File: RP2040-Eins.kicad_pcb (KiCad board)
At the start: 2 copper layers, 68.6 x 53.3 mm, 57 parts, among them J1 Barrel_Jack_Switch, J10 USB_C_Receptacle_USB2.0, J2 CONN_I, J3 CONN_A, J4 CONN_P, J5 CONN_X, J7 CONN_JTAG, J8 CONN_D1, J9 CONN_D2, Q1 AO3401A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

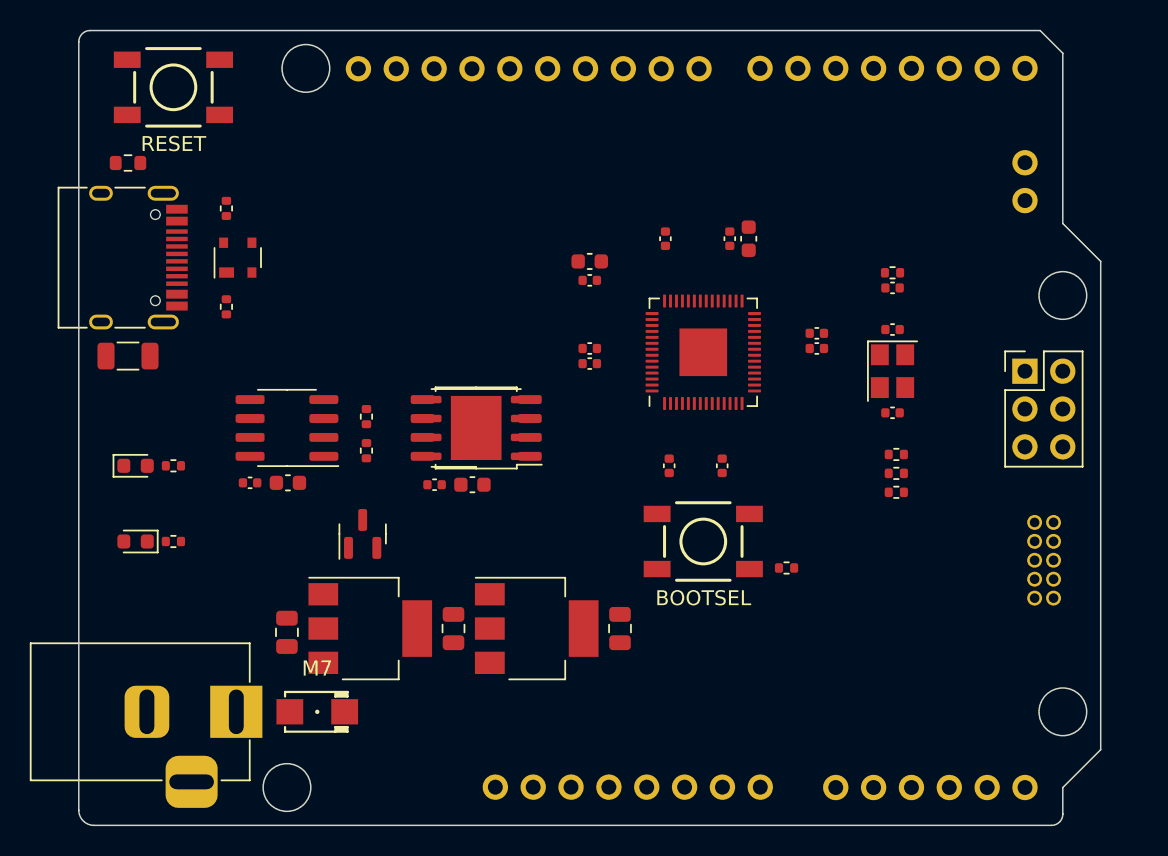
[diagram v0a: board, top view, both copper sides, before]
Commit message: Added few traces
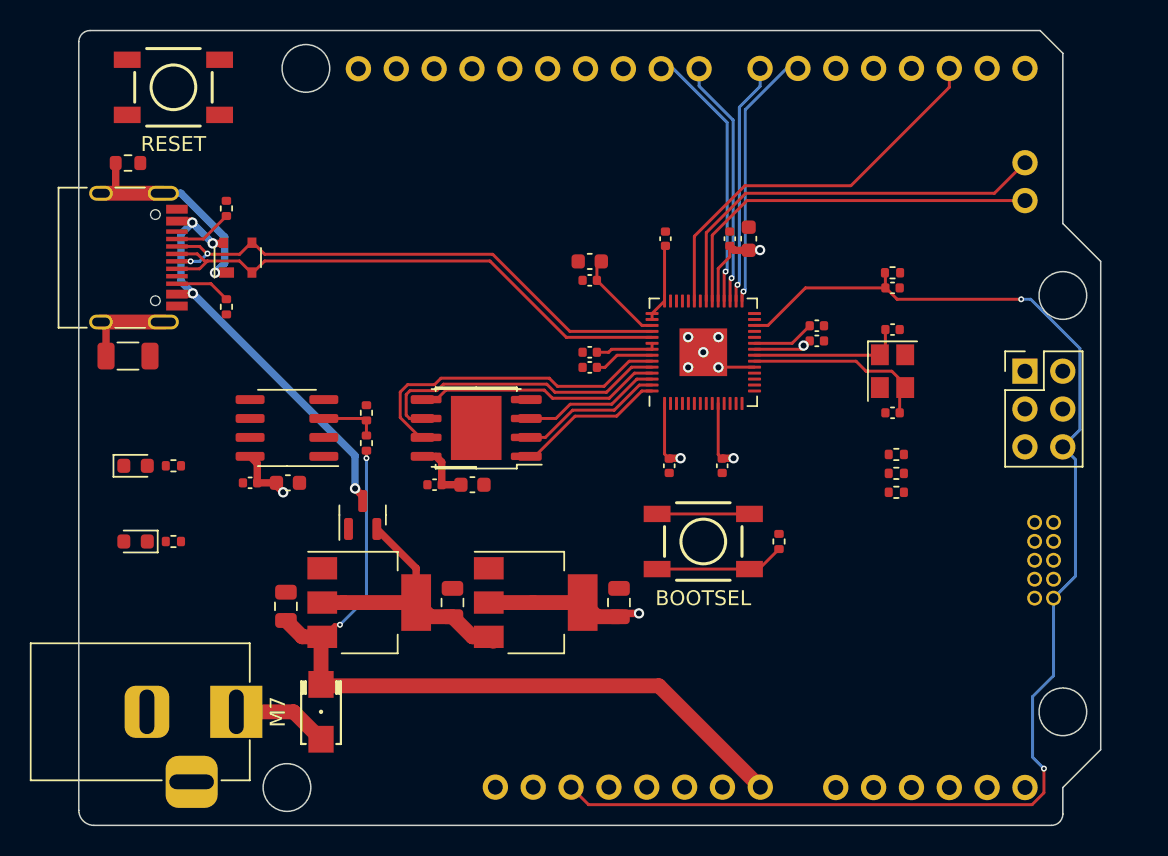
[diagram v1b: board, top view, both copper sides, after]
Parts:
- moved R7 1.85 mm to (174.0, 108.0), turned to 90 degrees
- moved C14 1.75 mm to (163.3, 112.0)
- moved U5 1.75 mm to (157.7, 112.0)
- moved C12 1.75 mm to (140.9, 112.3)
- moved C15 1.75 mm to (152.1, 112.0)
- moved U3 1.75 mm to (146.5, 112.0)
- moved Q1 1.27 mm to (146.1, 106.2)
- moved C7 0.51 mm to (176.5, 93.5)
- moved C6 0.51 mm to (176.5, 94.5)
- moved R8 0.51 mm to (146.3, 101.3)
- moved R9 0.26 mm to (146.3, 99.3)
- moved C10 0.25 mm to (161.3, 95.2)
- moved C22 0.25 mm to (161.3, 96.3)
- moved D4 0.25 mm to (143.3, 119.4), turned to -90 degrees
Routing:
- net RESET: track 0.00 -> 90.3 mm, vias 0 -> 2
- net VIN: track 0.00 -> 52.5 mm, vias 0 -> 2
- net +3V3: track 0.00 -> 42.7 mm, vias 0 -> 5
- net USB_DN: track 0.00 -> 37.2 mm, vias 0 -> 2
- net USB_DP: track 0.00 -> 37.1 mm
- net VBUS: track 0.00 -> 28.9 mm, vias 0 -> 4
- net D21: track 0.00 -> 27.9 mm
- net D2: track 0.00 -> 26.9 mm
- net D20: track 0.00 -> 26.4 mm
- net +5V: track 0.00 -> 22.7 mm, vias 0 -> 1
- net SHIELD: track 0.00 -> 22.4 mm, vias 0 -> 1
- net QSPI_SD3: track 0.00 -> 22.0 mm
- net QSPI_SCLK: track 0.00 -> 20.6 mm
- net D9: track 0.00 -> 18.0 mm, vias 0 -> 1
- net D6: track 0.00 -> 17.6 mm, vias 0 -> 1
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
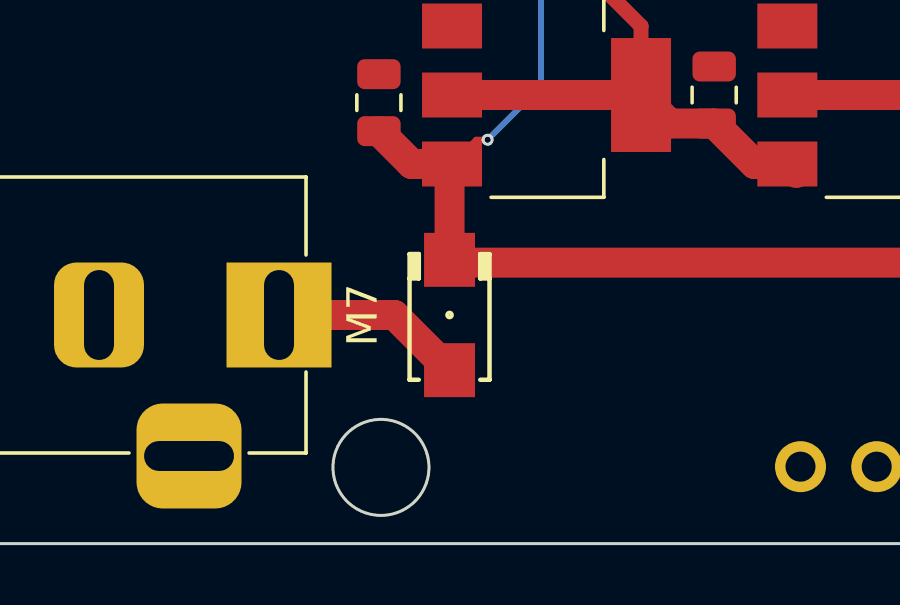
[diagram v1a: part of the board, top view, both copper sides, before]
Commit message: Put schottky diode instead of normal one.
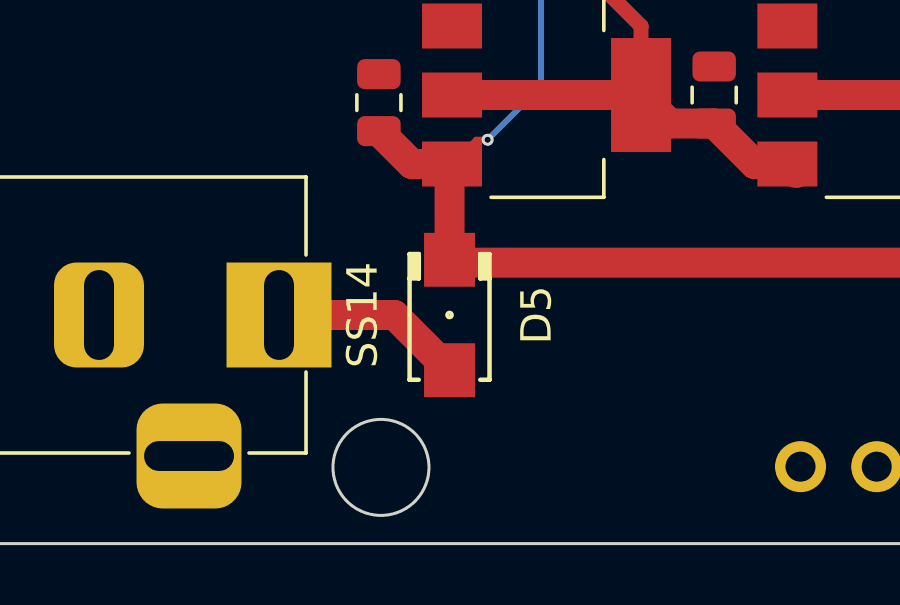
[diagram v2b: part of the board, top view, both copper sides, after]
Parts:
- removed D4: M7, PCM_4ms_Diode:D_DO-214AC_SMA
- added D5: SS14, PCM_4ms_Diode:D_DO-214AC_SMA, F.Cu at (143.3, 119.4)
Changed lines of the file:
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@@
   (net 64 "Net-(J10-CC2)")
   (net 65 "unconnected-(J10-SBU2-PadB8)")
-  (net 66 "Net-(D4-A)")
+  (net 66 "Net-(D5-A)")
   (footprint "Package_TO_SOT_SMD:SOT-23" (layer "F.Cu")
     (at 146.05 106.172 90)
@@
       (stroke (width 0.1) (type solid)) (layer "F.Fab"))
     (pad "1" thru_hole rect (at 0 0) (size 3.5 3.5) (drill oval 1 3) (layers "*.Cu" "*.Mask")
-      (net 66 "Net-(D4-A)") (pintype "passive"))
+      (net 66 "Net-(D5-A)") (pintype "passive"))
     (pad "2" thru_hole roundrect (at -6 0) (size 3 3.5) (drill oval 1 3) (layers "*.Cu" "*.Mask") (roundrect_rratio 0.25)
       (net 4 "GND") (pintype "passive"))
@@
     )
   )
+  (footprint "PCM_4ms_Diode:D_DO-214AC_SMA" (layer "F.Cu")
+    (at 143.256 119.38 -90)
+    (descr "Diode DO-214AC (SMA) Vishay")
+    (tags "Diode SMA")
+    (property "Sheetfile" "RP2040-Eins.kicad_sch")
+    (property "Sheetname" "")
+    (property "ki_description" "SMA Schottky diode, 40V, 1A, Alternate KiCAD Library")
+    (property "ki_keywords" "diode Schottky SS14")
+    (attr smd)
+    (fp_text reference "D5" (at 0 -2.9 90) (layer "F.SilkS")
+        (effects (font (size 1.016 1.016) (thickness 0.1524)))
+    )
+    (fp_text value "SS14" (at 0 2.9 90) (layer "F.SilkS")
+        (effects (font (size 1.016 1.016) (thickness 0.1524)))
+    )
+    (fp_line (start -2.032 -1.3325) (end -2.032 -1.0245)
+      (stroke (width 0.15) (type solid)) (layer "F.SilkS"))
+    (fp_line (start -2.032 -1.3325) (end 2.159 -1.3325)
+      (stroke (width 0.15) (type solid)) (layer "F.SilkS"))
+    (fp_line (start -2.032 1.3325) (end -2.032 1.0245)
+      (stroke (width 0.15) (type solid)) (layer "F.SilkS"))
+    (fp_line (start -2.032 1.3325) (end 2.159 1.3325)
+      (stroke (width 0.15) (type solid)) (layer "F.SilkS"))
+    (fp_line (start -1.9156 -1.18) (end -1.33 -1.18)
+      (stroke (width 0.3) (type solid)) (layer "F.SilkS"))
+    (fp_line (start -1.89 1.17) (end -1.34 1.17)
+      (stroke (width 0.3) (type solid)) (layer "F.SilkS"))
+    (fp_line (start -1.2192 -1.3325) (end -1.2192 -1.0245)
+      (stroke (width 0.15) (type solid)) (layer "F.SilkS"))
+    (fp_line (start -1.2192 -1.0245) (end -2.032 -1.0245)
+      (stroke (width 0.15) (type solid)) (layer "F.SilkS"))
+    (fp_line (start -1.2192 1.0245) (end -2.032 1.0245)
+      (stroke (width 0.15) (type solid)) (layer "F.SilkS"))
+    (fp_line (start -1.2192 1.3325) (end -1.2192 1.0245)
+      (stroke (width 0.15) (type solid)) (layer "F.SilkS"))
+    (fp_line (start 2.159 -1.3325) (end 2.159 -1.0245)
+      (stroke (width 0.15) (type solid)) (layer "F.SilkS"))
+    (fp_line (start 2.159 1.3325) (end 2.159 1.0245)
+      (stroke (width 0.15) (type solid)) (layer "F.SilkS"))
+    (fp_circle (center 0 0) (end 0.0762 -0.0254)
+      (stroke (width 0.127) (type solid)) (fill none) (layer "F.SilkS"))
+    (fp_line (start -3 -1.6575) (end 3 -1.6575)
+      (stroke (width 0.05) (type solid)) (layer "F.CrtYd"))
+    (fp_line (start -3 1.6575) (end -3 -1.6575)
+      (stroke (width 0.05) (type solid)) (layer "F.CrtYd"))
+    (fp_line (start 3 -1.6575) (end 3 1.6575)
+      (stroke (width 0.05) (type solid)) (layer "F.CrtYd"))
+    (fp_line (start 3 1.6575) (end -3 1.6575)
+      (stroke (width 0.05) (type solid)) (layer "F.CrtYd"))
+    (pad "1" smd rect (at -1.84 0 270) (size 1.8 1.7) (layers "F.Cu" "F.Paste" "F.Mask")
+      (net 5 "VIN") (pinfunction "K") (pintype "passive"))
+    (pad "2" smd rect (at 1.84 0 270) (size 1.8 1.7) (layers "F.Cu" "F.Paste" "F.Mask")
+      (net 66 "Net-(D5-A)") (pinfunction "A") (pintype "passive"))
+    (model "${KISYS3DMOD}/Diode_SMD.3dshapes/D_SMA.wrl"
+      (offset (xyz 0 0 0))
+      (scale (xyz 1 1 1))
+      (rotate (xyz 0 0 0))
+    )
+  )
   (footprint "Package_DFN_QFN:QFN-56-1EP_7x7mm_P0.4mm_EP3.2x3.2mm" (layer "F.Cu")
     (at 168.91 95.25 90)
@@
       (offset (xyz 0 0 0))
       (scale (xyz 1 1 1))
-      (rotate (xyz 0 0 0))
-    )
-  )
-  (footprint "PCM_4ms_Diode:D_DO-214AC_SMA" (layer "F.Cu")
-    (at 143.256 119.38 -90)
-    (descr "Diode DO-214AC (SMA) Vishay")
-    (tags "Diode SMA")
-    (property "Sheetfile" "RP2040-Eins.kicad_sch")
-    (property "Sheetname" "")
-    (property "ki_description" "SMA Diode, Rectifier, 1000V, 1A, Alternate KiCad Library")
-    (property "ki_keywords" "diode M7 4007")
-    (attr smd)
-    (fp_text reference "D4" (at 0 -2.9 -270) (layer "F.SilkS") hide
-        (effects (font (size 1.016 1.016) (thickness 0.1524)))
-    )
-    (fp_text value "M7" (at 0 2.9 -270) (layer "F.SilkS")
-        (effects (font (size 1.016 1.016) (thickness 0.1524)))
-    )
-    (fp_line (start -2.032 -1.3325) (end -2.032 -1.0245)
-      (stroke (width 0.15) (type solid)) (layer "F.SilkS"))
-    (fp_line (start -2.032 -1.3325) (end 2.159 -1.3325)
-      (stroke (width 0.15) (type solid)) (layer "F.SilkS"))
-    (fp_line (start -2.032 1.3325) (end -2.032 1.0245)
-      (stroke (width 0.15) (type solid)) (layer "F.SilkS"))
-    (fp_line (start -2.032 1.3325) (end 2.159 1.3325)
-      (stroke (width 0.15) (type solid)) (layer "F.SilkS"))
-    (fp_line (start -1.9156 -1.18) (end -1.33 -1.18)
-      (stroke (width 0.3) (type solid)) (layer "F.SilkS"))
-    (fp_line (start -1.89 1.17) (end -1.34 1.17)
-      (stroke (width 0.3) (type solid)) (layer "F.SilkS"))
-    (fp_line (start -1.2192 -1.3325) (end -1.2192 -1.0245)
-      (stroke (width 0.15) (type solid)) (layer "F.SilkS"))
-    (fp_line (start -1.2192 -1.0245) (end -2.032 -1.0245)
-      (stroke (width 0.15) (type solid)) (layer "F.SilkS"))
-    (fp_line (start -1.2192 1.0245) (end -2.032 1.0245)
-      (stroke (width 0.15) (type solid)) (layer "F.SilkS"))
-    (fp_line (start -1.2192 1.3325) (end -1.2192 1.0245)
-      (stroke (width 0.15) (type solid)) (layer "F.SilkS"))
-    (fp_line (start 2.159 -1.3325) (end 2.159 -1.0245)
-      (stroke (width 0.15) (type solid)) (layer "F.SilkS"))
-    (fp_line (start 2.159 1.3325) (end 2.159 1.0245)
-      (stroke (width 0.15) (type solid)) (layer "F.SilkS"))
-    (fp_circle (center 0 0) (end 0.0762 -0.0254)
-      (stroke (width 0.127) (type solid)) (fill none) (layer "F.SilkS"))
-    (fp_line (start -3 -1.6575) (end 3 -1.6575)
-      (stroke (width 0.05) (type solid)) (layer "F.CrtYd"))
-    (fp_line (start -3 1.6575) (end -3 -1.6575)
-      (stroke (width 0.05) (type solid)) (layer "F.CrtYd"))
-    (fp_line (start 3 -1.6575) (end 3 1.6575)
-      (stroke (width 0.05) (type solid)) (layer "F.CrtYd"))
-    (fp_line (start 3 1.6575) (end -3 1.6575)
-      (stroke (width 0.05) (type solid)) (layer "F.CrtYd"))
-    (pad "1" smd rect (at -1.84 0 270) (size 1.8 1.7) (layers "F.Cu" "F.Paste" "F.Mask")
-      (net 5 "VIN") (pinfunction "K") (pintype "passive"))
-    (pad "2" smd rect (at 1.84 0 270) (size 1.8 1.7) (layers "F.Cu" "F.Paste" "F.Mask")
-      (net 66 "Net-(D4-A)") (pinfunction "A") (pintype "passive"))
-    (model "${KISYS3DMOD}/Diode_SMD.3dshapes/D_SMA.wrl"
-      (offset (xyz 0 0 0))
-      (scale (xyz 1 1 1))

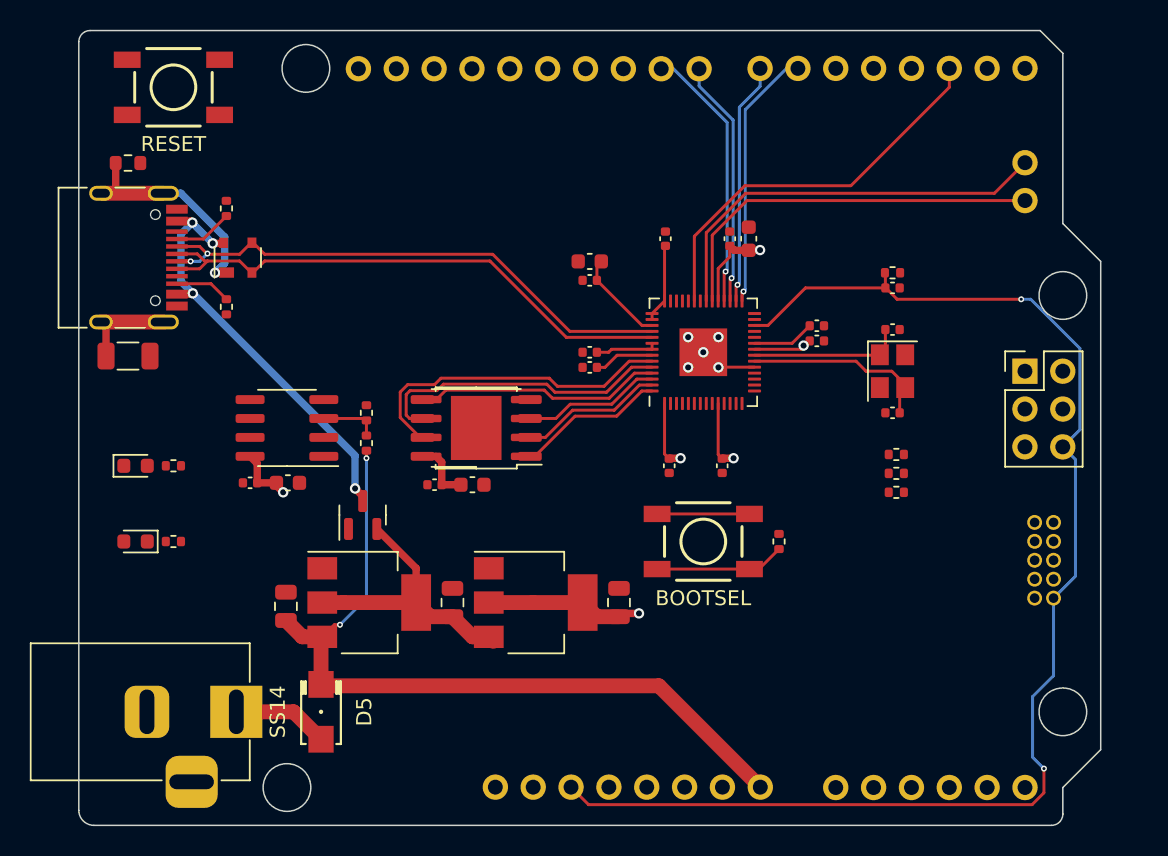
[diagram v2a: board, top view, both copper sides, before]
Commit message: Simplified the schematics a bit
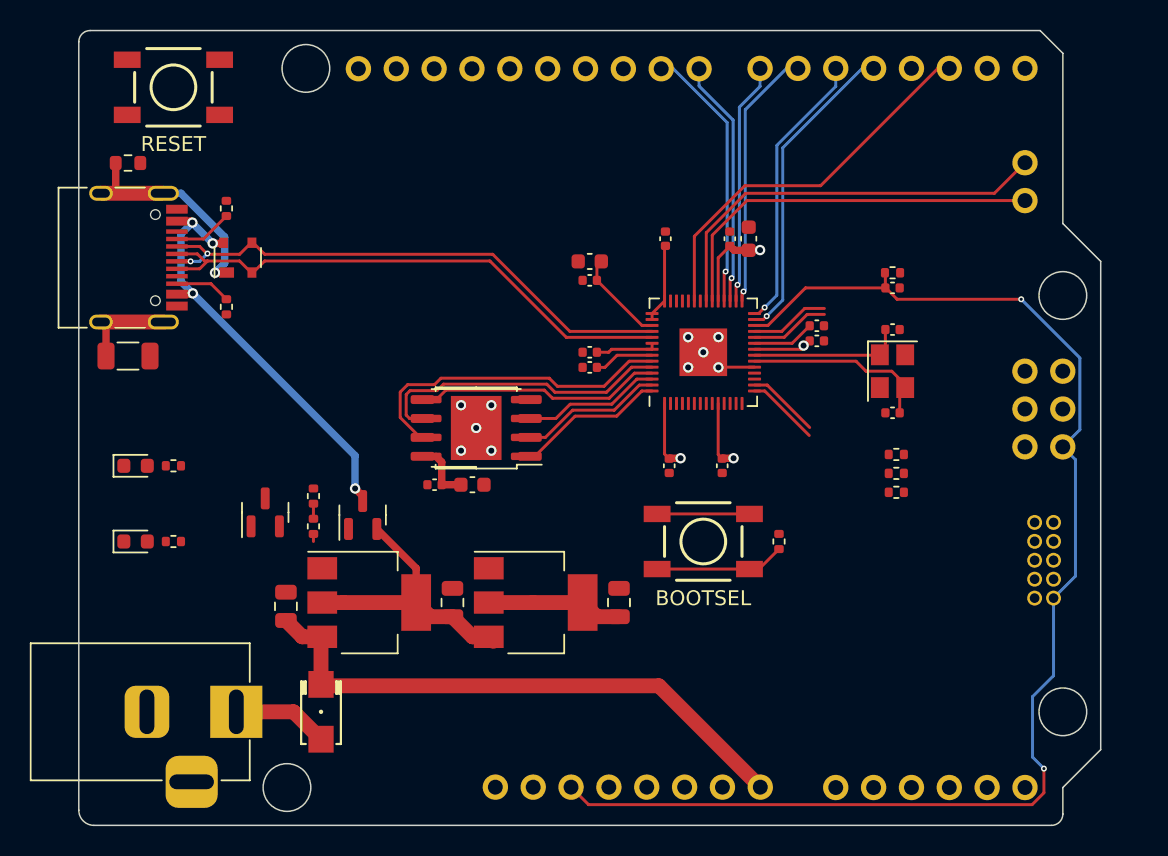
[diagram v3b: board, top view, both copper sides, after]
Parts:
- removed C17: 2.2uF, Capacitor_SMD:C_0603_1608Metric
- removed C18: 100nF, Capacitor_SMD:C_0402_1005Metric
- removed U6: LM358, Package_SO:SOIC-8_3.9x4.9mm_P1.27mm
- added Q2: AO3400A, Package_TO_SOT_SMD:SOT-23, F.Cu at (139.5, 106.0)
- J1: value Barrel_Jack_Switch -> CONN_PWR
- J10: value USB_C_Receptacle_USB2.0 -> CONN_USB
- J2: value CONN_I -> CONN_ICSP
- R1, R6: value 1k -> 5k1
- moved R9 6.62 mm to (142.7, 104.9)
- moved R8 6.62 mm to (142.7, 106.9)
- turned D2 to 0 degrees
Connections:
- D1 pad 1: GND -> Net-(D1-K)
- D2 pad 1: Net-(D2-K) -> GND
- D2 pad 2: +3V3 -> Net-(D2-A)
- R1 pad 1: Net-(U6B--) -> Net-(D1-A)
- R1 pad 2: Net-(D1-A) -> +3V3
- R6 pad 1: Net-(D2-K) -> +3V3
- R6 pad 2: GND -> Net-(D2-A)
- R8 pad 2: Net-(U6A-+) -> Net-(Q1-G)
- R9 pad 1: Net-(U6A-+) -> Net-(Q1-G)
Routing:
- net D4: track 0.00 -> 21.0 mm, vias 0 -> 1
- net D5: track 0.00 -> 18.9 mm, vias 0 -> 1
- net VIN: track 52.5 -> 39.0 mm, vias 2 -> 0
- net SWCLK: track 0.00 -> 5.33 mm
- net SWD: track 0.00 -> 5.33 mm
- net D18_SDA: track 0.00 -> 4.91 mm
- net D19_SCL: track 0.00 -> 4.88 mm
- net +5V: track 22.7 -> 18.6 mm, vias 1 -> 0
- net Net-(U6A-+): track 3.92 -> 0.00 mm
- net +3V3: track 42.7 -> 41.3 mm, vias 5 -> 4
- net Net-(Q1-G): track 0.00 -> 1.19 mm
- net D2: track 26.9 -> 26.1 mm
- net GND: vias 5 -> 10
